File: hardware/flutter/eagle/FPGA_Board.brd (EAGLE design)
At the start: 100 x 77 mm, 60 parts, among them IC1 AT45DB161D-SU, IC2 MEGA8-AI, IC3 MAX3468CSA, Q1 8Mhz, U2 XC3S50AVQ100

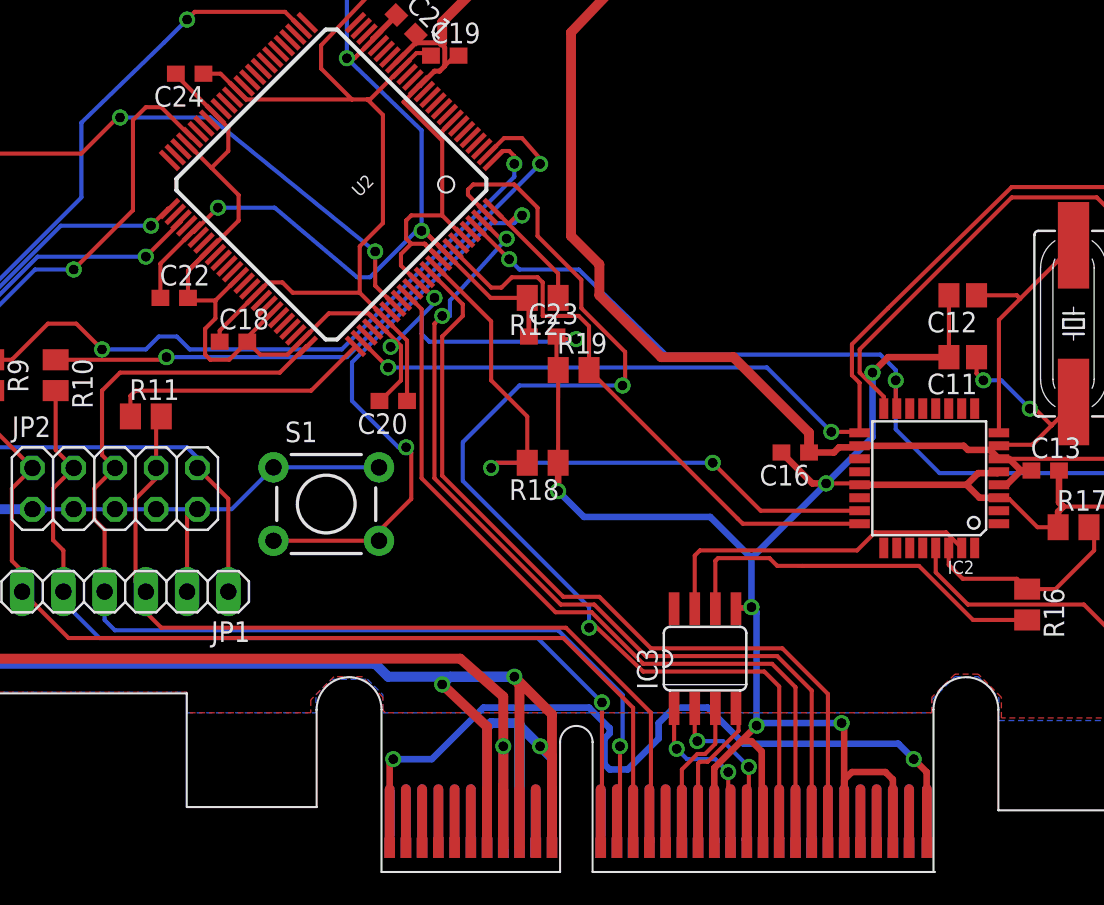
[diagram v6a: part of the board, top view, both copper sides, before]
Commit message: changed level converter for rs48 from max488 to max481 (similar to max485)
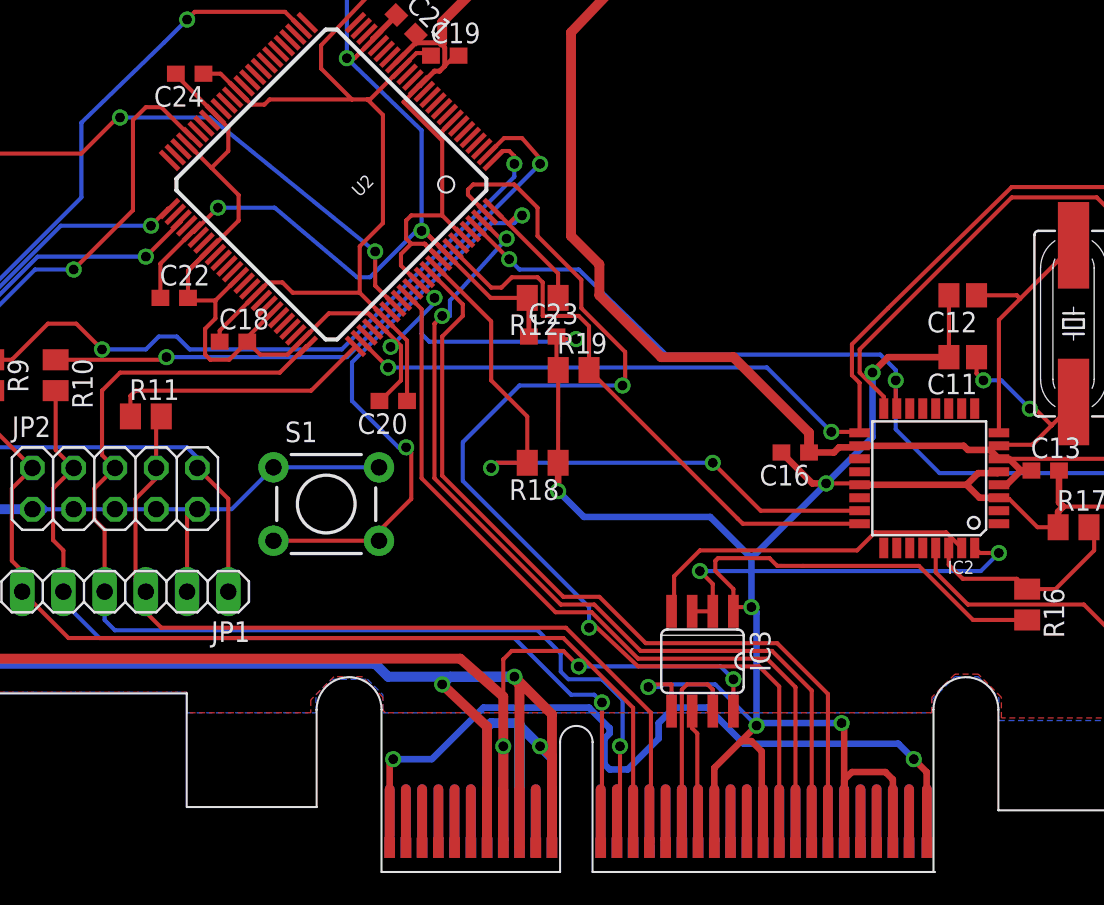
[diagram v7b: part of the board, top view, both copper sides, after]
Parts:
- IC3: value MAX3468CSA -> MAX481CSA
- moved IC3 0.22 mm to (64.8, 12.2), turned to 180 degrees
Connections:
- removed net UC_RX+: IC3.4, U$4.A18(TX+)
- removed net UC_RX-: IC3.3, U$4.A17(TX-)
- removed net UC_TX+: IC3.1, U$4.A20(RX+)
- removed net UC_TX-: IC3.2, U$4.A21(RX-)
- new net BUS0+: IC3.6, U$4.A18(BUS0+)
- new net BUS0-: IC3.7, U$4.A17(BUS0-)
- new net BUS1+: U$4.A20(BUS1+)
- new net BUS1-: U$4.A21(BUS1-)
- net +5V: now also IC3.8
- net N$10: now also IC3.1; no longer IC3.6
- net N$5: now also IC2.32, IC3.2, IC3.3; no longer IC3.8
- net N$6: now also IC3.4; no longer IC3.7
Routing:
- net N$5: track 0.00 -> 24.6 mm, vias 0 -> 2
- net +5V: track 274.7 -> 294.1 mm, vias 1 -> 3
- net BUS0-: track 0.00 -> 13.2 mm
- net UC_TX+: track 11.0 -> 0.00 mm, vias 2 -> 0
- net UC_TX-: track 10.9 -> 0.00 mm, vias 2 -> 0
- net GND: track 681.4 -> 691.5 mm, vias 14 -> 15
- net UC_RX+: track 9.95 -> 0.00 mm
- net UC_RX-: track 9.70 -> 0.00 mm
- net BUS0+: track 0.00 -> 8.56 mm
- net N$6: track 20.7 -> 21.4 mm
- net N$10: track 23.8 -> 24.4 mm

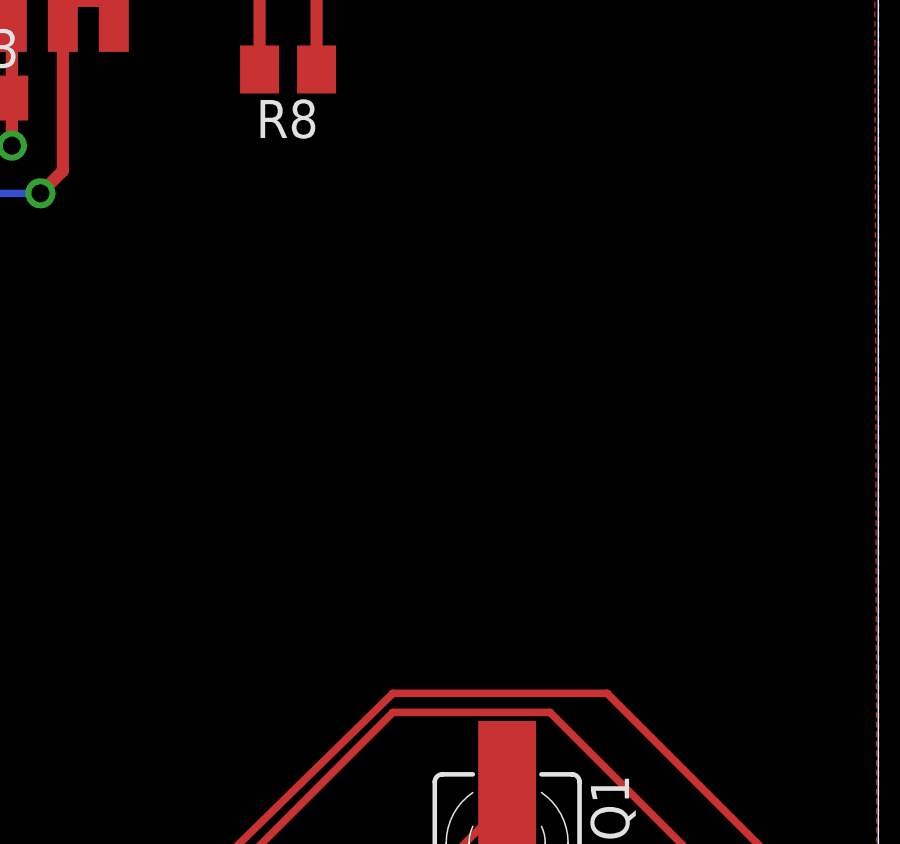
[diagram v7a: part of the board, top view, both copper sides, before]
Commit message: added GPS module to hgg.lbr and circuit of fpga timing board
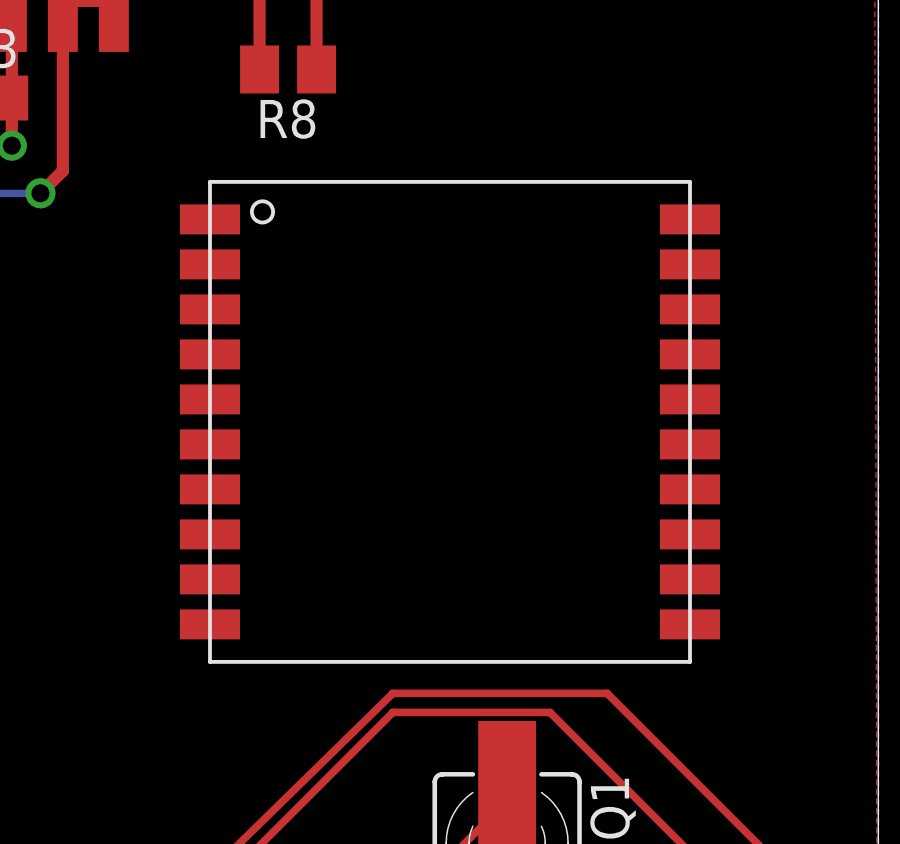
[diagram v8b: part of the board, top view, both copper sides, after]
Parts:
- added U$6: GPS, hgg:GPS
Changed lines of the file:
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@@
 <attribute name="OC_FARNELL" value="unknown" x="64.77" y="12.22375" size="1.778" layer="27" rot="R180" display="off"/>
 </element>
+<element name="U$6" library="hgg" package="GPS" value="GPS" x="85.725" y="50.4825"/>
 </elements>
 <signals>
